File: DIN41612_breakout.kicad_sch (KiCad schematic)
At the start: 1 part, among them J1 09031967921

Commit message: Add DIP switches
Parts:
- added R15, R16: 120Ω, PCM_JLCPCB:R_1206, symbol PCM_JLCPCB-Resistors:1206,120Ω
- added S1: DIP Switch x 2, PCM_JLCPCB:SW-SMD_218-2LPSTRF, symbol PCM_JLCPCB-Connectors_Buttons:DIP Switch x 2
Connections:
- net CAN1.+: now also R15.2
- net USB.+ renamed USB_DIN.D+
- net USB.- renamed USB_DIN.D-
- new net: R16.1, S1.2
- new net: R15.1, S1.1

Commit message: Fix paths
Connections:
- net CAN1.-: now also S1.4
- net CAN2.+: now also S1.3
- net CAN2.-: now also R16.2
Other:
- moved on the sheet: R15, R16, S1

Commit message: Fix USB connection
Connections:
- net USB_DIN.D+ renamed USB_DIN.+
- net USB_DIN.D- renamed USB_DIN.-
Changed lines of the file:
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@@
+	)
+	(bus_entry
+		(at 228.6 129.54)
+		(size 2.54 -2.54)
+		(stroke
+			(width 0)
+			(type default)
+		)
 	)
 	(bus_entry
@@
 	)
 	(bus_entry
-		(at 234.95 132.08)
-		(size -2.54 -2.54)
-		(stroke
-			(width 0)
-			(type default)
-		)
-	)
-	(bus_entry
 		(at 83.82 171.45)
 		(size -2.54 2.54)
+		(stroke
+			(width 0)
+			(type default)
+		)
+	)
+	(bus_entry
+		(at 228.6 132.08)
+		(size 2.54 -2.54)
 		(stroke
 			(width 0)
@@
 	)
 	(bus_entry
-		(at 234.95 129.54)
-		(size -2.54 -2.54)
-		(stroke
-			(width 0)
-			(type default)
-		)
-	)
-	(bus_entry
 		(at 213.36 44.45)
 		(size 2.54 2.54)
@@
 	(bus
 		(pts
-			(xy 234.95 129.54) (xy 234.95 132.08)
-		)
-		(stroke
-			(width 0)
-			(type default)
-		)
-	)
-	(bus
-		(pts
 			(xy 81.28 87.63) (xy 81.28 90.17)
 		)
@@
 		)
 	)
-	(bus
-		(pts
-			(xy 234.95 132.08) (xy 234.95 135.89)
-		)
-		(stroke
-			(width 0)
-			(type default)
-		)
-	)
 	(wire
 		(pts
@@
 		)
 	)
-	(wire
-		(pts
-			(xy 213.36 127) (xy 232.41 127)
-		)
-		(stroke
-			(width 0)
-			(type default)
-		)
-	)
 	(bus
 		(pts
@@
 	(wire
 		(pts
+			(xy 252.73 129.54) (xy 231.14 129.54)
+		)
+		(stroke
+			(width 0)
+			(type default)
+		)
+	)
+	(wire
+		(pts
 			(xy 107.95 49.53) (xy 107.95 52.07)
 		)
@@
 	(bus
 		(pts
+			(xy 220.98 139.7) (xy 228.6 139.7)
+		)
+		(stroke
+			(width 0)
+			(type default)
+		)
+	)
+	(bus
+		(pts
 			(xy 215.9 74.93) (xy 215.9 77.47)
 		)
@@
 		)
 	)
+	(bus
+		(pts
+			(xy 228.6 132.08) (xy 228.6 139.7)
+		)
+		(stroke
+			(width 0)
+			(type default)
+		)
+	)
 	(wire
 		(pts
@@
 	(wire
 		(pts
+			(xy 252.73 127) (xy 231.14 127)
+		)
+		(stroke
+			(width 0)
+			(type default)
+		)
+	)
+	(wire
+		(pts
 			(xy 83.82 44.45) (xy 133.35 44.45)
 		)
@@
 	(bus
 		(pts
-			(xy 240.03 135.89) (xy 234.95 135.89)
+			(xy 228.6 129.54) (xy 228.6 132.08)
 		)
 		(stroke
@@
 		(pts
 			(xy 133.35 90.17) (xy 83.82 90.17)
-		)
-		(stroke
-			(width 0)
-			(type default)
-		)
-	)
-	(wire
-		(pts
-			(xy 213.36 129.54) (xy 232.41 129.54)
 		)
 		(stroke
@@
 		)
 	)
+	(label "USB_DIN.+"
+		(at 100.33 26.67 0)
+		(effects
+			(font
+				(size 1.27 1.27)
+			)
+			(justify left bottom)
+		)
+	)
 	(label "GPIOC5"
 		(at 95.25 158.75 0)
@@
 		)
 	)
-	(label "USB_DIN.D+"
-		(at 100.33 26.67 0)
-		(effects
-			(font
-				(size 1.27 1.27)
-				(italic yes)
-			)
-			(justify left bottom)
-		)
-	)
 	(label "GPIOR3"
 		(at 195.58 69.85 0)
@@
 		)
 	)
+	(label "USB_DIN.-"
+		(at 195.58 26.67 180)
+		(effects
+			(font
+				(size 1.27 1.27)
+			)
+			(justify right bottom)
+		)
+	)
 	(label "GPIOR6"
 		(at 195.58 77.47 0)
@@
 		)
 	)
-	(label "USB_DIN.D-"
-		(at 195.58 26.67 180)
-		(effects
-			(font
-				(size 1.27 1.27)
-				(italic yes)
+	(label "USB_DIN.+"
+		(at 252.73 127 180)
+		(effects
+			(font
+				(size 1.27 1.27)
 			)
 			(justify right bottom)
@@
 		)
 	)
-	(label "USB_DIN.D+"
-		(at 213.36 127 0)
-		(effects
-			(font
-				(size 1.27 1.27)
-			)
-			(justify left bottom)
-		)
-	)
-	(label "USB_DIN.D-"
-		(at 213.36 129.54 0)
-		(effects
-			(font
-				(size 1.27 1.27)
-			)
-			(justify left bottom)
-		)
-	)
 	(label "GPIOR11"
 		(at 195.58 90.17 0)
@@
 			)
 			(justify left bottom)
+		)
+	)
+	(label "USB_DIN.-"
+		(at 252.73 129.54 180)
+		(effects
+			(font
+				(size 1.27 1.27)
+			)
+			(justify right bottom)
 		)
 	)
@@
 		)
 	)
-	(hierarchical_label "USB_DIN{USB}"
+	(hierarchical_label "USB_DIN{+ -}"
 		(shape input)
-		(at 240.03 135.89 0)
-		(effects
-			(font
-				(size 1.27 1.27)
-			)
-			(justify left)
-		)
-	)
+		(at 220.98 139.7 180)
+		(effects
+			(font
+				(size 1.27 1.27)
+			)
+			(justify right)
+		)
+	)

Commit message: Change DIP switch footprint
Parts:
- S1: footprint PCM_JLCPCB:SW-SMD_218-2LPSTRF -> Button_Switch_THT:SW_DIP_SPSTx02_Slide_9.78x7.26mm_W7.62mm_P2.54mm
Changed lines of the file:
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@@
 			)
 		)
-		(property "Footprint" "PCM_JLCPCB:SW-SMD_218-2LPSTRF"
+		(property "Footprint" "Button_Switch_THT:SW_DIP_SPSTx02_Slide_9.78x7.26mm_W7.62mm_P2.54mm"
 			(at 53.34 54.61 0)
 			(effects

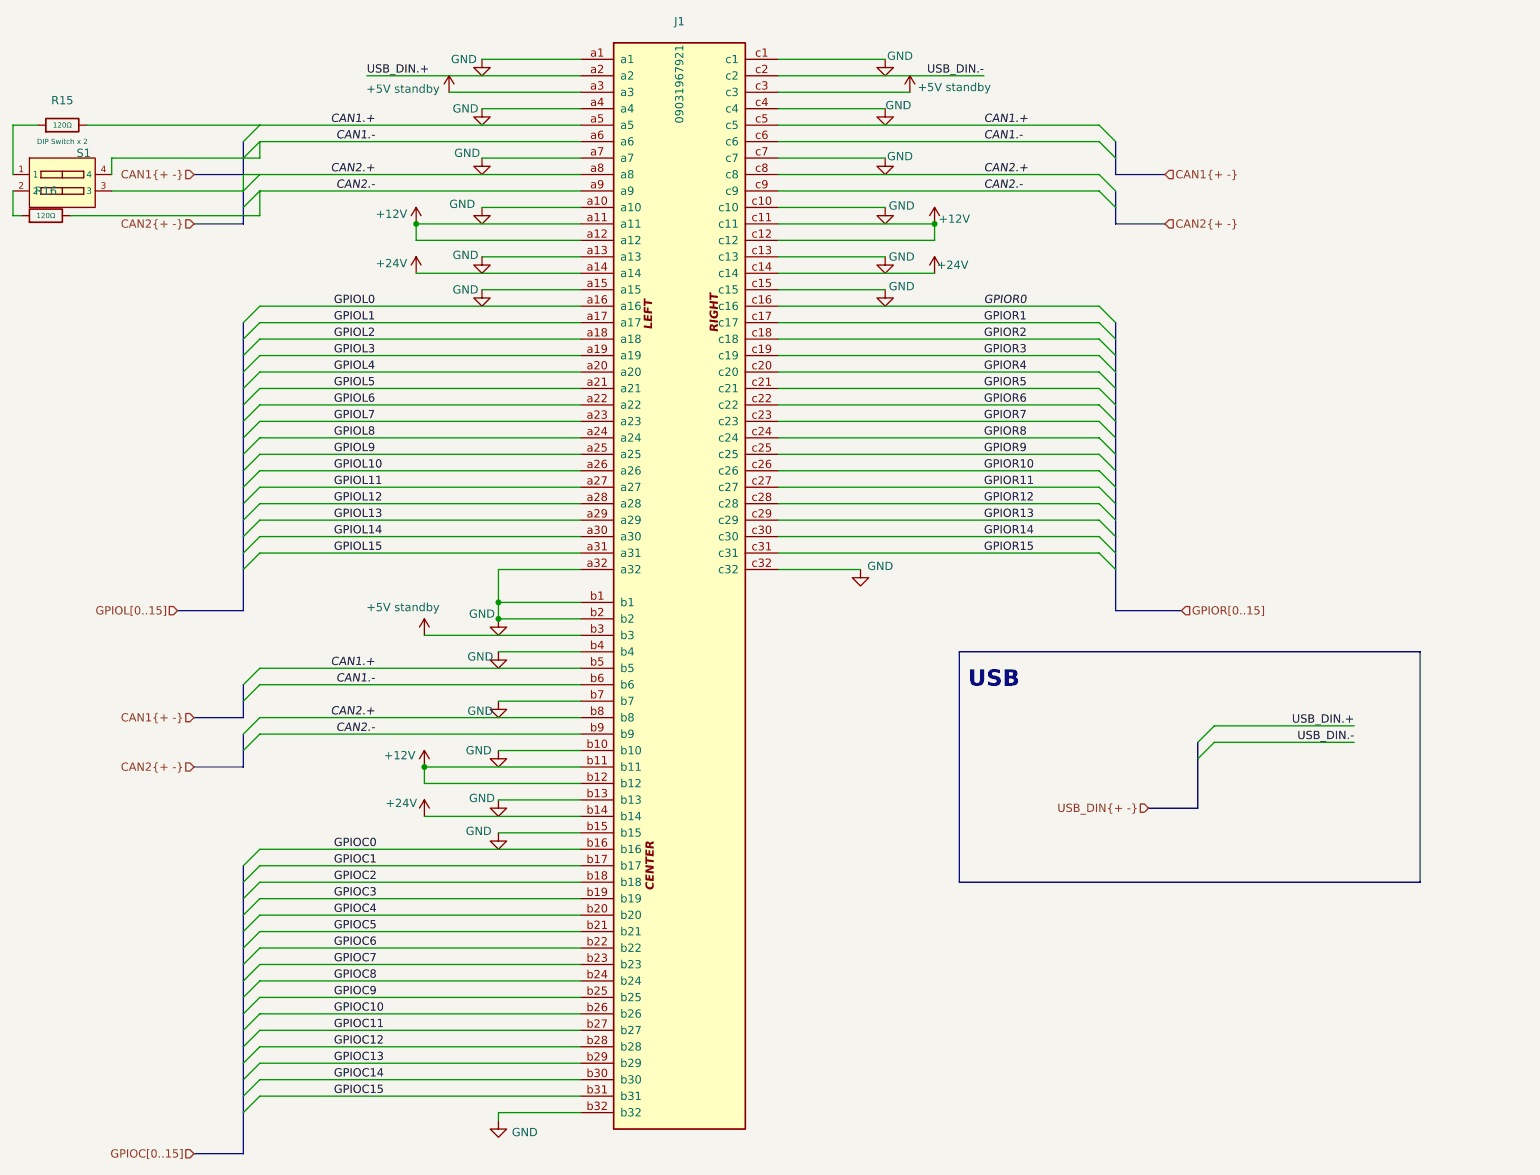
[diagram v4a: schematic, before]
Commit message: Change DIP switch connection
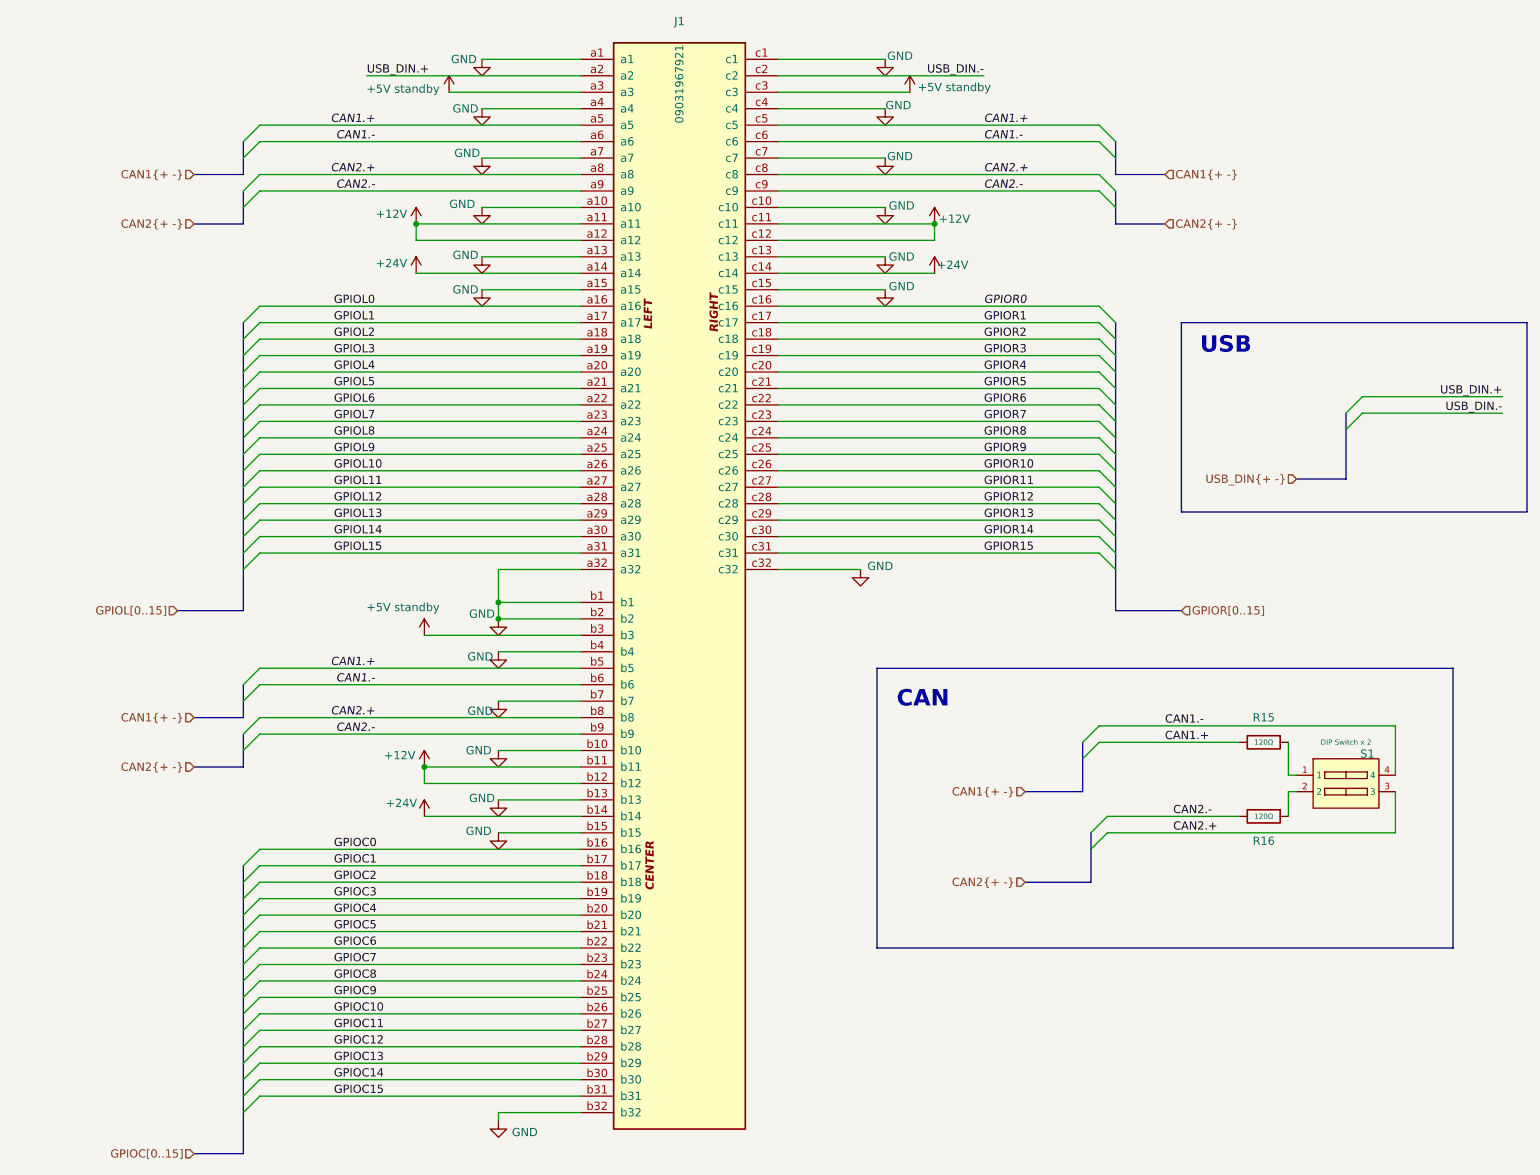
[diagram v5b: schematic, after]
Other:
- note added: "CAN"
- moved on the sheet: R15, R16, S1

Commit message: Change schematic
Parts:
- removed R15, R16: 120Ω, PCM_JLCPCB:R_1206, symbol PCM_JLCPCB-Resistors:1206,120Ω
- added R15, R16: 120Ω, PCM_JLCPCB:R_0603, symbol PCM_JLCPCB-Resistors:0603,120Ω
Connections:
- net CAN1.+: now also R15.1
- net CAN2.-: now also R16.1
- net at S1.2: now also R16.2
- net at S1.1: now also R15.2
